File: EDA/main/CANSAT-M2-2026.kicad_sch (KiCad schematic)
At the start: 1 part, among them U7 STM32H7S3L8H6

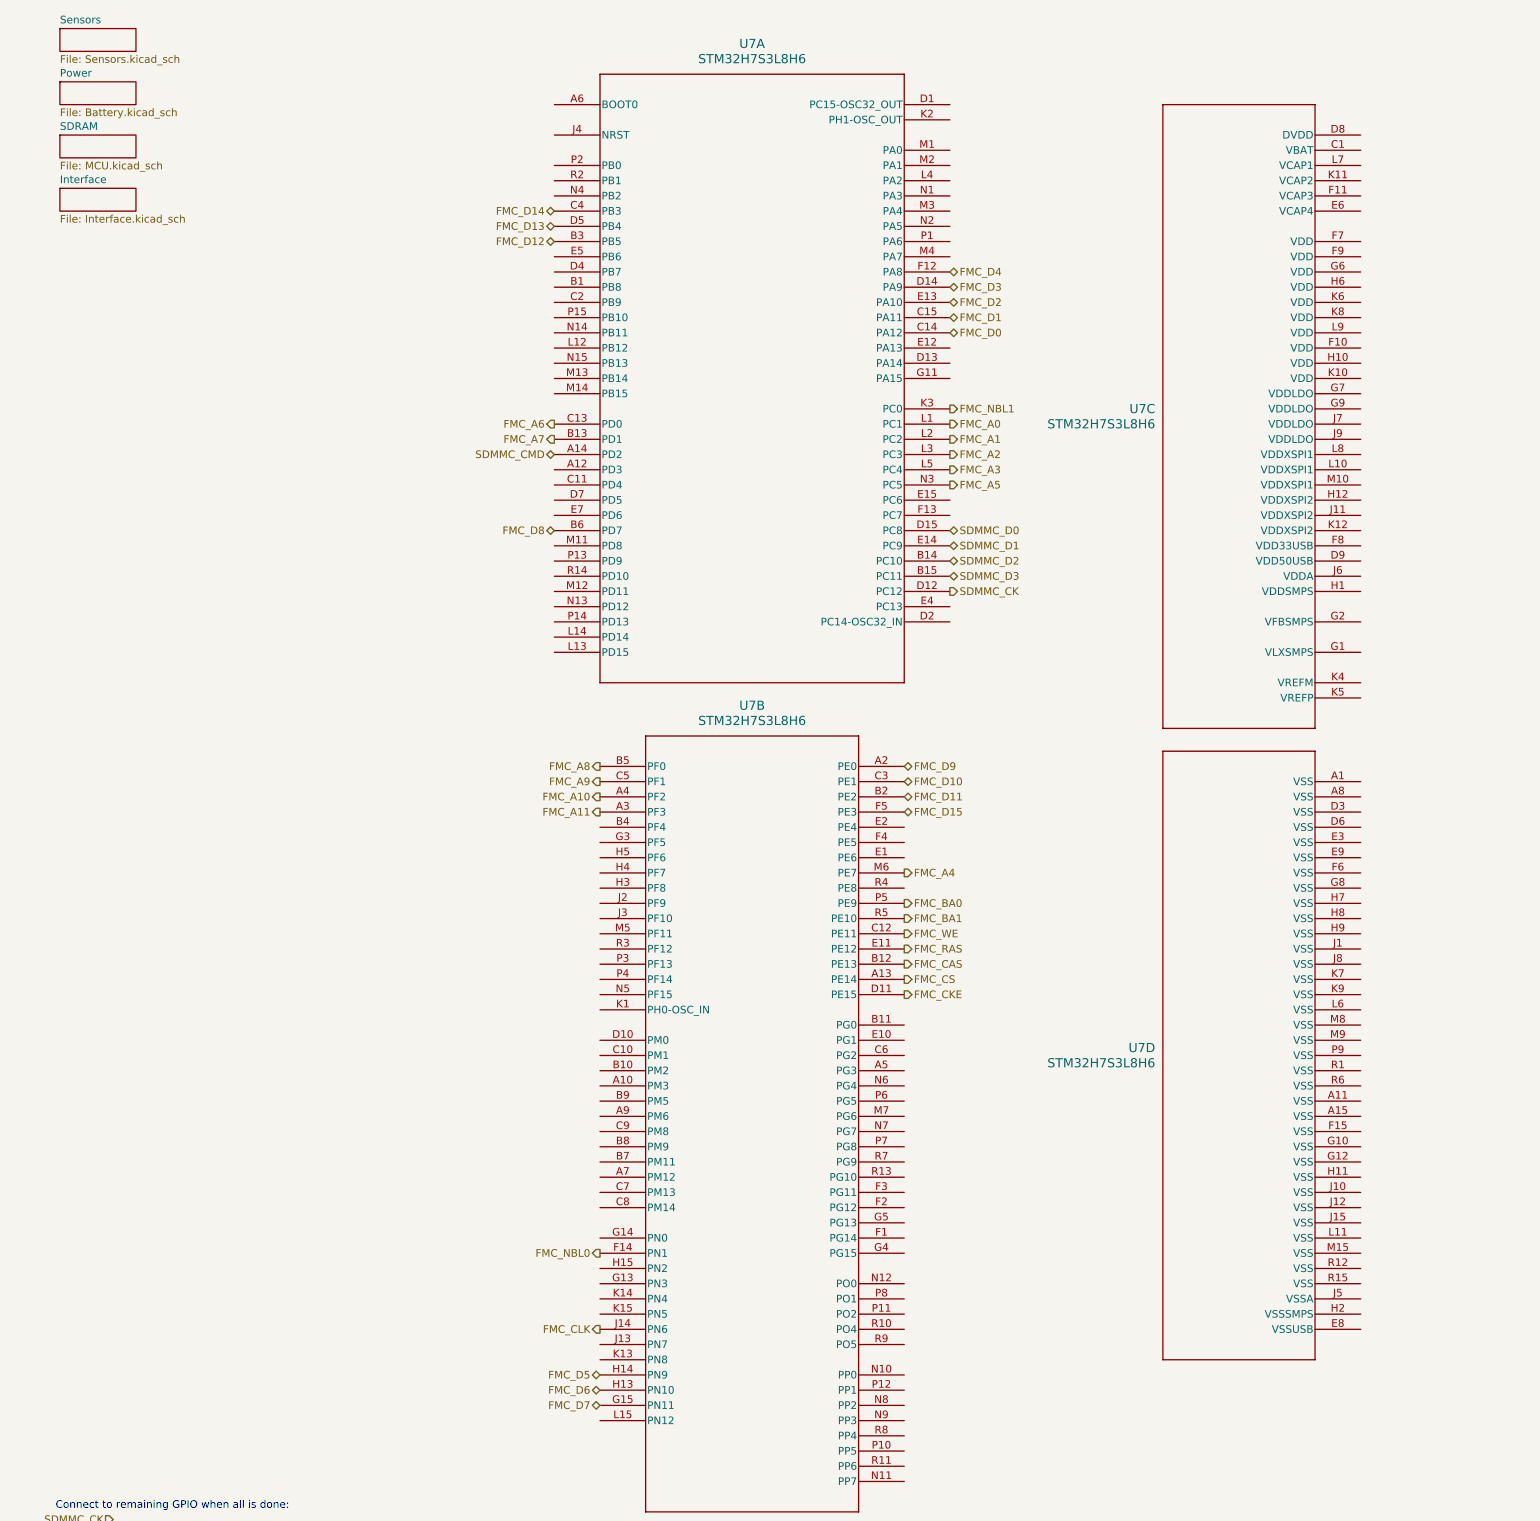
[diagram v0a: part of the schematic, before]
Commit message: Project restructure, and added a bottom assembly PCB.
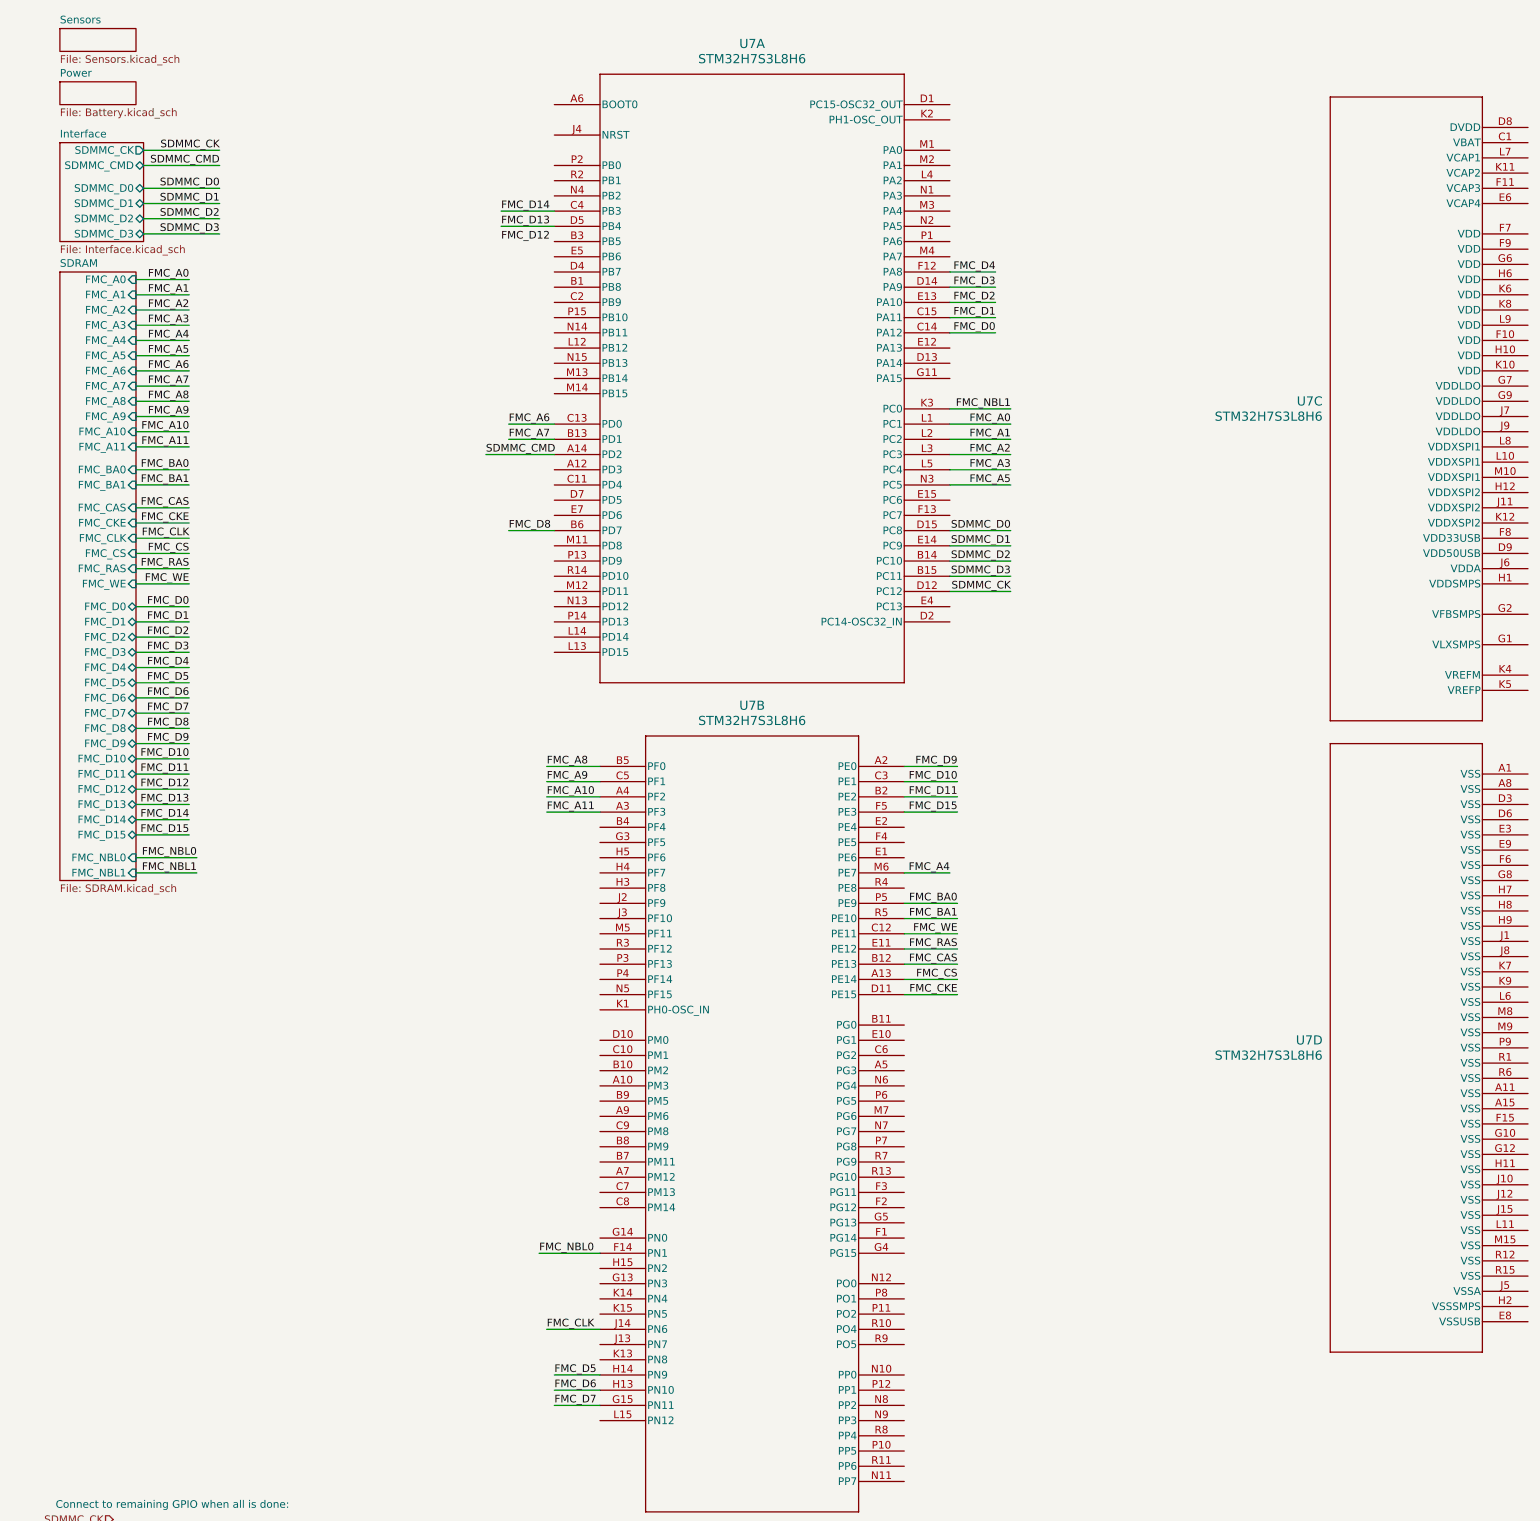
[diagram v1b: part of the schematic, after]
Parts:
- U7: footprint TFBGA225_13X13_STM -> CANSAT-lib:TFBGA225_13X13_STM
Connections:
- net FMC_D12: no longer U7.B3 (PB5)
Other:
- sheet Interface ports: added SDMMC_CK, SDMMC_CMD, SDMMC_D0, SDMMC_D1, SDMMC_D2, SDMMC_D3; removed none
- sheet SDRAM: file MCU.kicad_sch -> SDRAM.kicad_sch
- sheet SDRAM ports: added FMC_A0, FMC_A1, FMC_A10, FMC_A11, FMC_A2, FMC_A3, FMC_A4, FMC_A5, FMC_A6, FMC_A7, FMC_A8, FMC_A9, FMC_BA0, FMC_BA1, FMC_CAS, FMC_CKE, FMC_CLK, FMC_CS, FMC_D0, FMC_D1, FMC_D10, FMC_D11, FMC_D12, FMC_D13, FMC_D14, FMC_D15, FMC_D2, FMC_D3, FMC_D4, FMC_D5, FMC_D6, FMC_D7, FMC_D8, FMC_D9, FMC_NBL0, FMC_NBL1, FMC_RAS, FMC_WE; removed none
- moved on the sheet: U7C, U7D

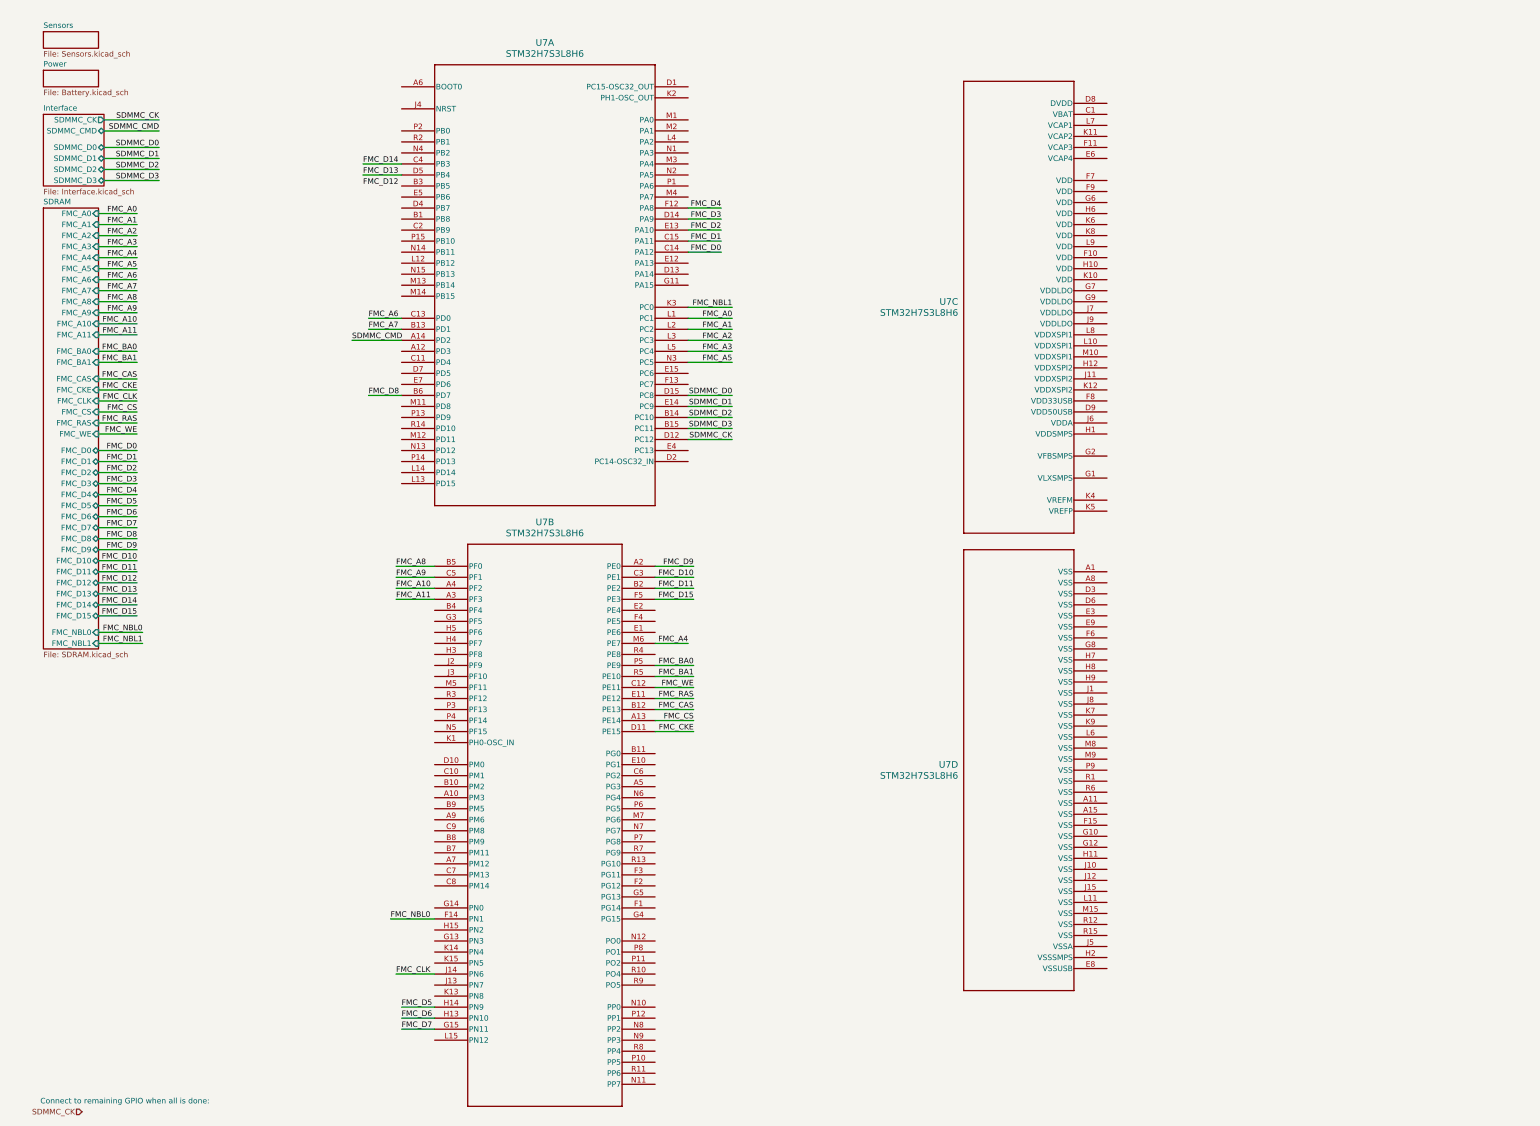
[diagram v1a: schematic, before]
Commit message: Assigned CS and INT from sensors, and added SWD to PWR-MCU and CORE-MCU
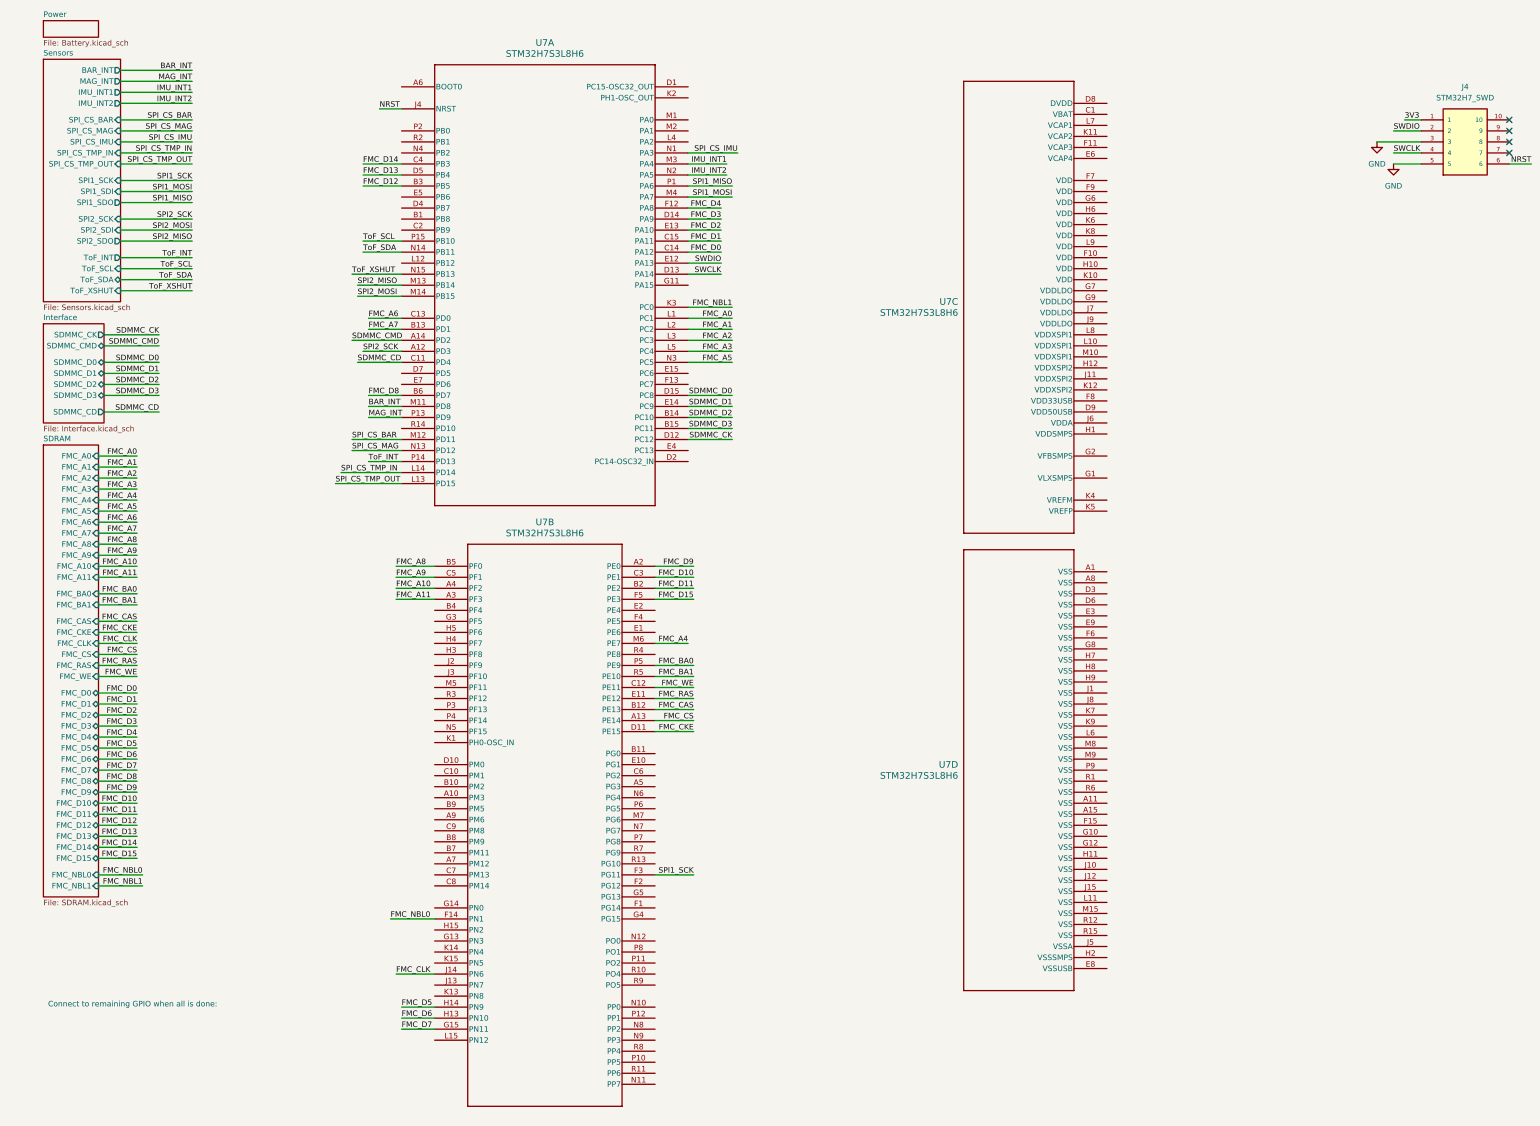
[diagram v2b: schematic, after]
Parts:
- added J4: STM32H7_SWD, CANSAT-lib:TAG-CONNECT_TC2050-IDC, symbol CANSAT-lib:TC2050-IDC
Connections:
- net FMC_D12: now also U7.B3 (PB5)
- net SPI1_SCK: now reaches U7.F3 (PG11)
- net SPI2_SCK: now reaches U7.A12 (PD3)
- net SDMMC_CD: now reaches U7.C11 (PD4)
- net SWCLK: now reaches U7.D13 (PA14)
- net SWCLK: now also J4.4
- net SWDIO: now reaches U7.E12 (PA13)
- net SWDIO: now also J4.2
- net NRST: now reaches U7.J4 (NRST)
- net NRST: now also J4.6
- net SPI_CS_TMP_OUT: now reaches U7.L13 (PD15)
- net SPI_CS_TMP_IN: now reaches U7.L14 (PD14)
- net BAR_INT: now reaches U7.M11 (PD8)
- net SPI_CS_BAR: now reaches U7.M12 (PD11)
- net SPI2_MISO: now reaches U7.M13 (PB14)
- net SPI2_MOSI: now reaches U7.M14 (PB15)
- net IMU_INT1: now reaches U7.M3 (PA4)
- net SPI1_MOSI: now reaches U7.M4 (PA7)
- net SPI_CS_IMU: now reaches U7.N1 (PA3)
- net SPI_CS_MAG: now reaches U7.N13 (PD12)
- net ToF_SDA: now reaches U7.N14 (PB11)
- net ToF_XSHUT: now reaches U7.N15 (PB13)
- net IMU_INT2: now reaches U7.N2 (PA5)
- net SPI1_MISO: now reaches U7.P1 (PA6)
- net MAG_INT: now reaches U7.P13 (PD9)
- net ToF_INT: now reaches U7.P14 (PD13)
- net ToF_SCL: now reaches U7.P15 (PB10)
- new net 3V3: J4.1
- new net GND: J4.3, J4.5
- no-connect marks 0 -> 4
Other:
- sheet Interface ports: added SDMMC_CD; removed none
- sheet Sensors ports: added BAR_INT, IMU_INT1, IMU_INT2, MAG_INT, SPI1_SCK, SPI1_SDI, SPI1_SDO, SPI2_SCK, SPI2_SDI, SPI2_SDO, SPI_CS_BAR, SPI_CS_IMU, SPI_CS_MAG, SPI_CS_TMP_IN, SPI_CS_TMP_OUT, ToF_INT, ToF_SCL, ToF_SDA, ToF_XSHUT; removed none

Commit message: Uploaded work
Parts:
- added C51, C52, C53, C54, C55, C56, C57, C58, C59, C61, C63, C65, C7, C71, C72, C73, C74, C75, C76, C79, C81: 100nF, Capacitor_SMD:C_0402_1005Metric, symbol Device:C
- added C60, C62, C70, C78: 4.7uF, Capacitor_SMD:C_0603_1608Metric, symbol Device:C
- added C64, C77, C80, C82: 1uF, Capacitor_SMD:C_0603_1608Metric, symbol Device:C
- added C66, C67, C68, C69: 2.2uF, Capacitor_SMD:C_0603_1608Metric, symbol Device:C
- added C83, C84: 10pF, Capacitor_SMD:C_0402_1005Metric, symbol Device:C
- added C85, C86: 18pF, Capacitor_SMD:C_0402_1005Metric, symbol Device:C
- added FB1: FerriteBead, symbol Device:FerriteBead
- added J6: SKRPACE010, CANSAT-lib:SW_SKRPACE010_AAL, symbol CANSAT-lib:SKRPACE010
- added R29: 10kΩ, Resistor_SMD:R_0402_1005Metric, symbol Device:R
- added Y2: 25MHz, CANSAT-lib:XTAL_ECS-160-9-37-CKM-TR, symbol CANSAT-lib:ECS-250-10-37B-CTN-TR
- added Y3: ABS07-32.768KHZ-T, CANSAT-lib:XTAL_ABS07-32.768KHZ-T, symbol CANSAT-lib:ABS07-32.768KHZ-T
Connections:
- net 3V3 is gone; now on net GND: J4.1
- net FMC_D12: now also U7.F5 (PE3); no longer U7.B3 (PB5)
- net FMC_D13: now also U7.E2 (PE4); no longer U7.D5 (PB4)
- net FMC_D14: now also U7.F4 (PE5); no longer U7.C4 (PB3)
- net FMC_D15: now also U7.E1 (PE6); no longer U7.F5 (PE3)
- net GND: now also U7.A1 (VSS), U7.A11 (VSS), U7.A15 (VSS), U7.A8 (VSS), U7.D3 (VSS), U7.D6 (VSS), U7.D9 (VDD50USB), U7.E3 (VSS), U7.E8 (VSSUSB), U7.E9 (VSS), U7.F10 (VDD), U7.F15 (VSS), U7.F6 (VSS), U7.F7 (VDD), U7.F8 (VDD33USB), U7.F9 (VDD), U7.G10 (VSS), U7.G12 (VSS), U7.G2 (VFBSMPS), U7.G6 (VDD), U7.G7 (VDDLDO), U7.G8 (VSS), U7.G9 (VDDLDO), U7.H1 (VDDSMPS), U7.H10 (VDD), U7.H11 (VSS), U7.H12 (VDDXSPI2), U7.H2 (VSSSMPS), U7.H6 (VDD), U7.H7 (VSS), U7.H8 (VSS), U7.H9 (VSS), U7.J1 (VSS), U7.J10 (VSS), U7.J11 (VDDXSPI2), U7.J12 (VSS), U7.J15 (VSS), U7.J5 (VSSA), U7.J7 (VDDLDO), U7.J8 (VSS), U7.J9 (VDDLDO), U7.K10 (VDD), U7.K12 (VDDXSPI2), U7.K4 (VREFM), U7.K6 (VDD), U7.K7 (VSS), U7.K8 (VDD), U7.K9 (VSS), U7.L10 (VDDXSPI1), U7.L11 (VSS), U7.L6 (VSS), U7.L8 (VDDXSPI1), U7.L9 (VDD), U7.M10 (VDDXSPI1), U7.M15 (VSS), U7.M8 (VSS), U7.M9 (VSS), U7.P9 (VSS), U7.R1 (VSS), U7.R12 (VSS), U7.R15 (VSS), U7.R6 (VSS), C51.1, C51.2, C52.1, C52.2, C53.1, C53.2, C54.1, C54.2, C55.1, C55.2, C56.1, C56.2, C57.1, C57.2, C58.1, C58.2, C59.1, C59.2, C60.1, C60.2, C61.1, C62.1, C62.2, C63.1, C63.2, C64.1, C64.2, C65.1, C65.2, C66.1, C67.1, C68.1, C69.1, C7.1, C7.2, C70.1, C71.1, C71.2, C72.1, C72.2, C73.1, C73.2, C74.1, C74.2, C75.1, C75.2, C76.1, C76.2, C77.1, C77.2, C78.1, C78.2, C79.2, C80.2, C81.2, C82.2, C83.1, C84.1, C85.1, C86.1, FB1.1, J6.2, R29.2, Y2.2 (GND), Y2.4 (GND)
- net at U7.C1 (VBAT): now also U7.D8 (DVDD), C61.2, C70.2
- net at U7.E6 (VCAP4): now also C66.2
- net at U7.F11 (VCAP3): now also C67.2
- net VDDA: now reaches U7.J6 (VDDA)
- net VDDA: now also U7.K5 (VREFP), C79.1, C80.1, C81.1, C82.1, FB1.2
- net at U7.K11 (VCAP2): now also C68.2
- net at U7.L7 (VCAP1): now also C69.2
- net HSE-OSC_IN: now reaches U7.K1 (PH0-OSC_IN)
- net HSE-OSC_IN: now also C83.2, Y2.3 (OUT/IN)
- net SENS_EN: now reaches U7.N12 (PO0)
- net BOOT0: now reaches U7.A6 (BOOT0)
- net BOOT0: now also J6.3, R29.1
- net LSE-OSC_OUT: now reaches U7.D1 (PC15-OSC32_OUT)
- net LSE-OSC_OUT: now also C86.2, Y3.1
- net LSE-OSC_IN: now reaches U7.D2 (PC14-OSC32_IN)
- net LSE-OSC_IN: now also C85.2, Y3.2
- net SPI_CS_PWR-MCU: now reaches U7.D4 (PB7)
- net SPI3_SDI: now reaches U7.E7 (PD6)
- net HSE-OSC_OUT: now reaches U7.K2 (PH1-OSC_OUT)
- net HSE-OSC_OUT: now also C84.2, Y2.1 (IN/OUT)
- new net SPI3_SCK: U7.C4 (PB3)
- new net SPI3_SDO: U7.D5 (PB4)
- no-connect marks 4 -> 7
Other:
- sheet Interface ports: added 3V3; removed none
- sheet Power ports: added 3V3, SPI_CS_PWR-MCU, SPI_SCK, SPI_SDI, SPI_SDO; removed none
- sheet SDRAM ports: added 3V3; removed none
- sheet Sensors ports: added 3V3, SENS_EN; removed none
- moved on the sheet: J4, U7C, U7D
